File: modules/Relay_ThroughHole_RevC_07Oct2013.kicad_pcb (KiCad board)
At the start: 2 copper layers, 14 parts

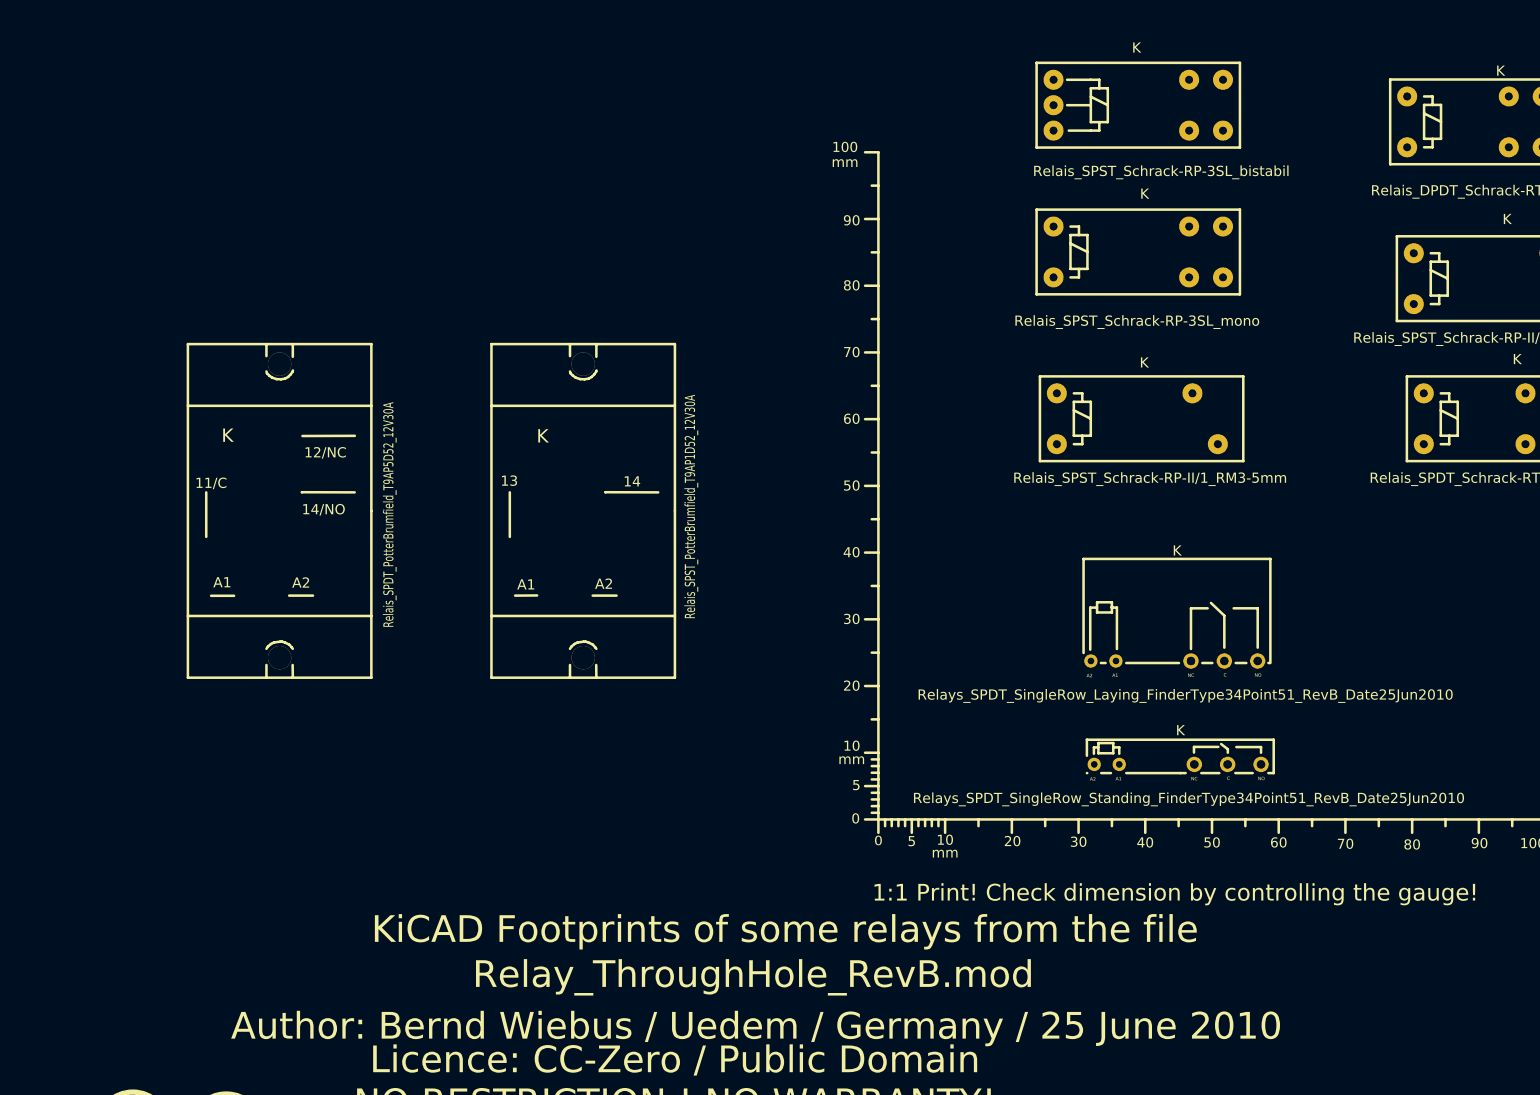
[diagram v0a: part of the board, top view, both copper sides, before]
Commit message: Some RP3SL relay update. LQFP48/TQFP48 footprints added.
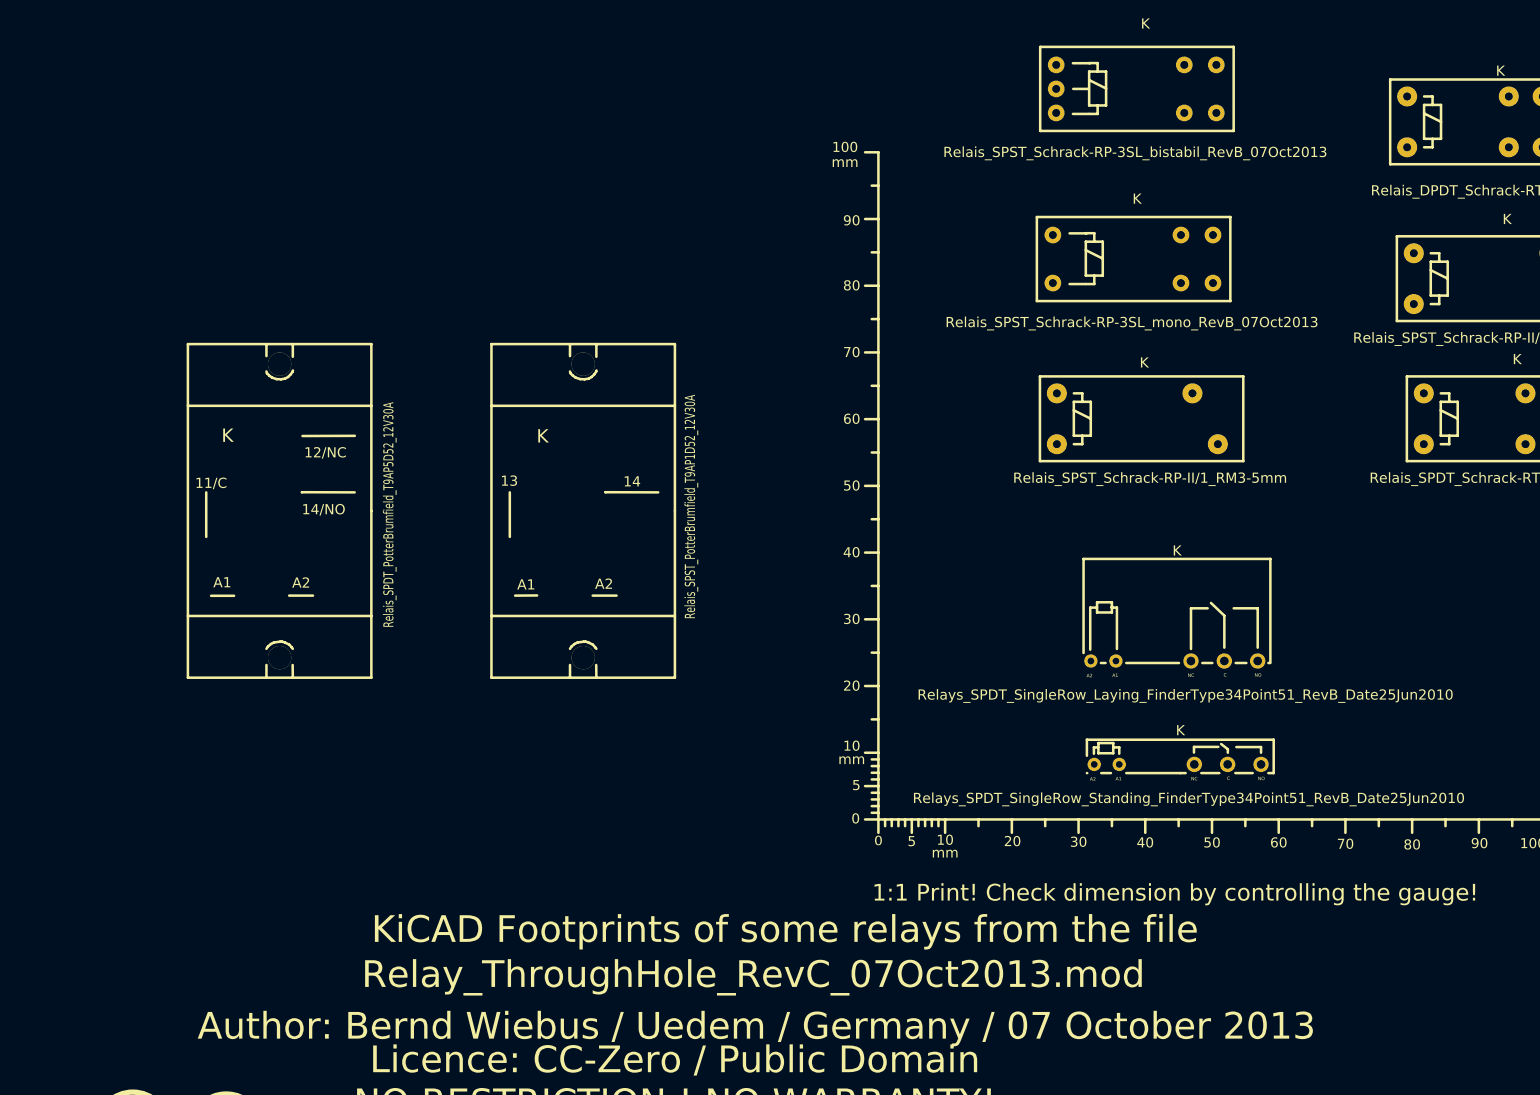
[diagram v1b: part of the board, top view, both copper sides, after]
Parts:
- removed the K at (159.0, 38.0)
- removed the K at (159.0, 60.0)
- added K: Relais_SPST_Schrack-RP-3SL_bistabil_RevB_07Oct2013, Relais_SPST_Schrack-RP-3SL_bistabil_RevB_07Oct2013, F.Cu at (171.5, 31.8)
- added K: Relais_SPST_Schrack-RP-3SL_mono_RevB_07Oct2013, Relais_SPST_Schrack-RP-3SL_mono_RevB_07Oct2013, F.Cu at (171.0, 57.2)
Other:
- board text added: "Author: Bernd Wiebus / Uedem / Germany / 07 October 2013"
- board text added: "Relay_ThroughHole_RevC_07Oct2013.mod"
- board text removed: "Author: Bernd Wiebus / Uedem / Germany / 25 June 2010"
- board text removed: "Relay_ThroughHole_RevB.mod"
